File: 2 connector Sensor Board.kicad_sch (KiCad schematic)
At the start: 12 parts, among them J1 SPI, J15 TE 3-2363962-0 Connector, J2 FPC 0.3mm Aces 51688-0070M, J3 Prog Pins, J4 TE 3-2363962-0 Connector, J5 FPC 0.3mm Aces 51688-0070M, J6 Free Pins, J7 JST SH

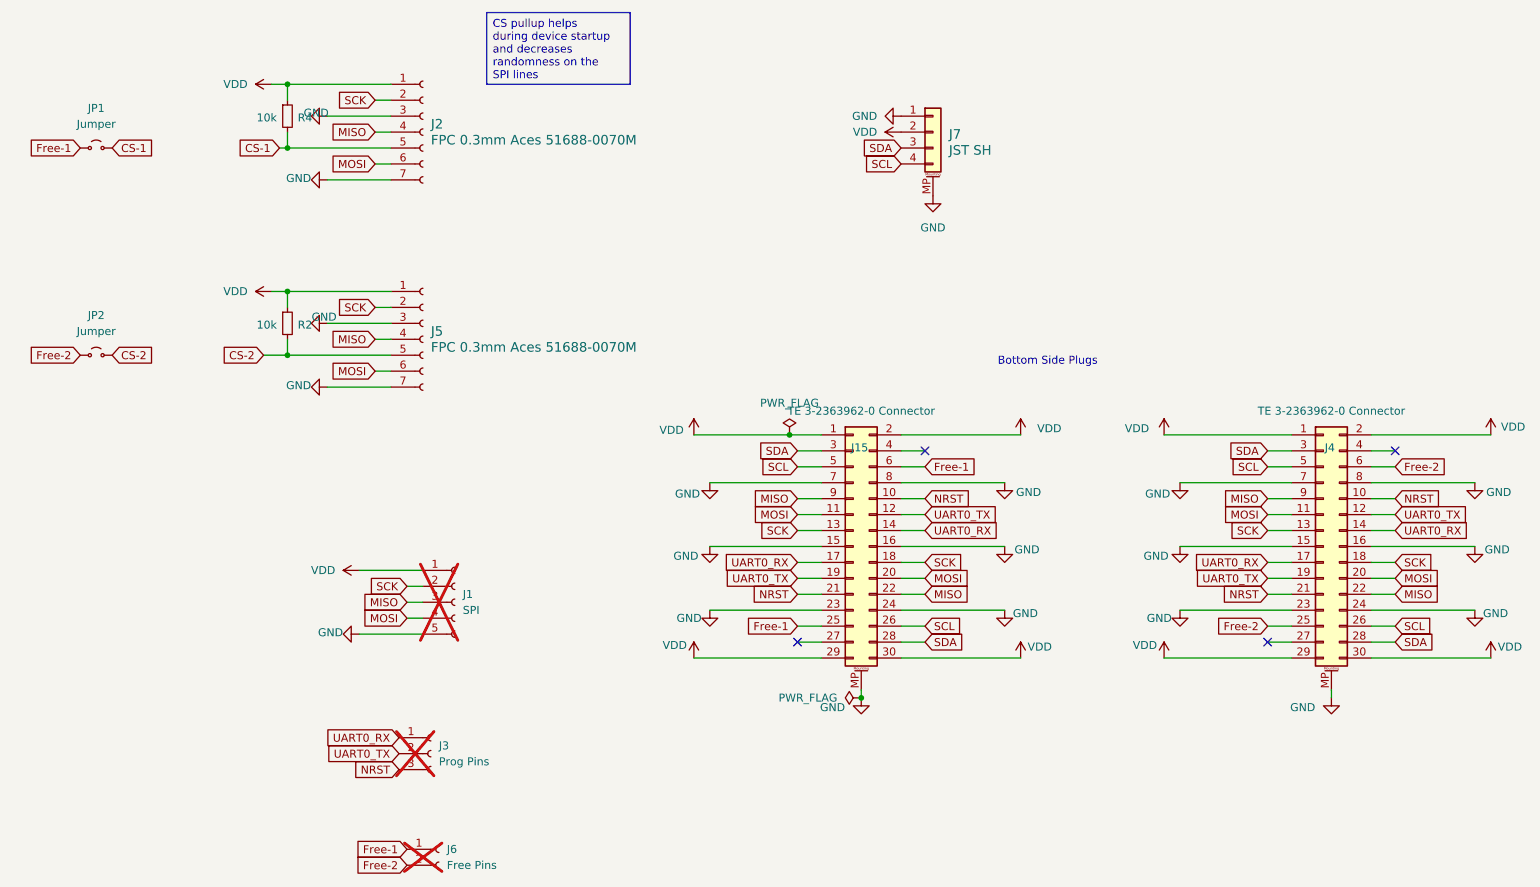
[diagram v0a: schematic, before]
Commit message: Finished reroute
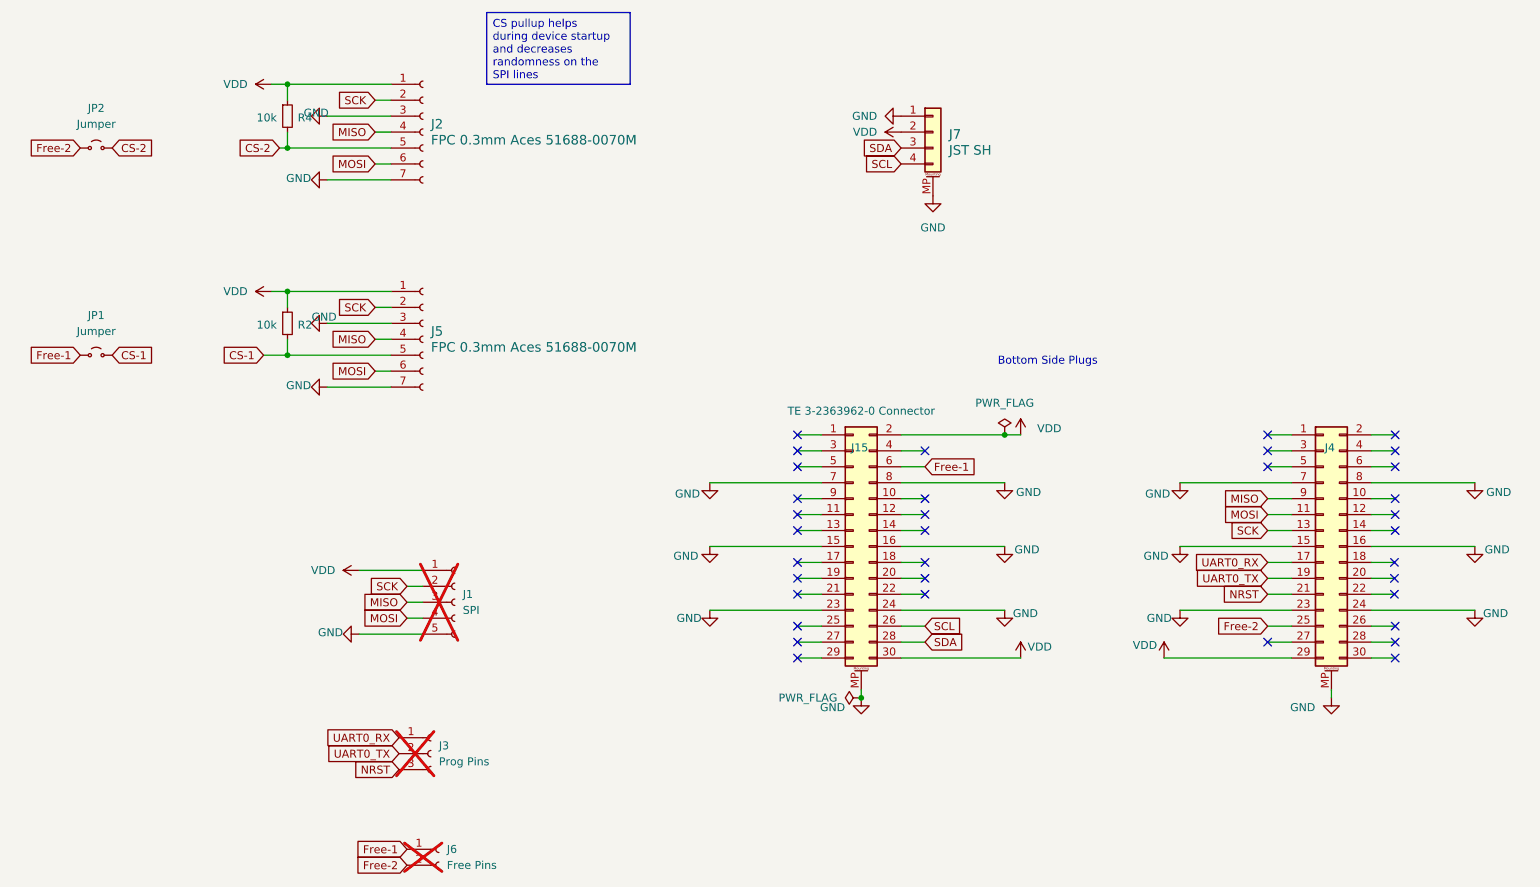
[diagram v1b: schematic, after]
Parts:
- renumbered JP2 to JP1, JP1 to JP2
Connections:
- net CS-1: now also J5.5 (Pin_5), JP1.2 (B), R2.2; no longer J2.5 (Pin_5), JP2.2 (B), R4.2
- net CS-2: now also J2.5 (Pin_5), JP2.2 (B), R4.2; no longer J5.5 (Pin_5), JP1.2 (B), R2.2
- net Free-1: now also JP1.1 (A); no longer J15.25 (Pin_25), JP2.1 (A)
- net Free-2: now also JP2.1 (A); no longer J4.6 (Pin_6), JP1.1 (A)
- net MISO: no longer J15.22 (Pin_22), J15.9 (Pin_9), J4.22 (Pin_22)
- net MOSI: no longer J15.11 (Pin_11), J15.20 (Pin_20), J4.20 (Pin_20)
- net NRST: no longer J15.10 (Pin_10), J15.21 (Pin_21), J4.10 (Pin_10)
- net SCK: no longer J15.13 (Pin_13), J15.18 (Pin_18), J4.18 (Pin_18)
- net SCL: no longer J15.5 (Pin_5), J4.26 (Pin_26), J4.5 (Pin_5)
- net SDA: no longer J15.3 (Pin_3), J4.28 (Pin_28), J4.3 (Pin_3)
- net UART0_RX: no longer J15.14 (Pin_14), J15.17 (Pin_17), J4.14 (Pin_14)
- net UART0_TX: no longer J15.12 (Pin_12), J15.19 (Pin_19), J4.12 (Pin_12)
- net VDD: no longer J15.1 (Pin_1), J15.29 (Pin_29), J4.1 (Pin_1), J4.2 (Pin_2), J4.30 (Pin_30)
- no-connect marks 4 -> 35
